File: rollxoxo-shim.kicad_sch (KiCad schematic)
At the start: 70 parts, among them J1 Conn_01x10, J2 USB_C_Receptacle_USB2.0_14P, J3 Conn_01x02, J5 Conn_01x01, J6 Conn_01x10, J7 Conn_01x03, J8 Conn_01x01, SW1 SW_Push, SW2 SW_Push, U1 SN74LV1T125DBV, U2 ESP32-S3FN8, U3 SN74LV1T125DBV, U4 SN74LV1T125DBV, U5 TPSM84338, U6 SN74LV1T125DBV, Y1 48M

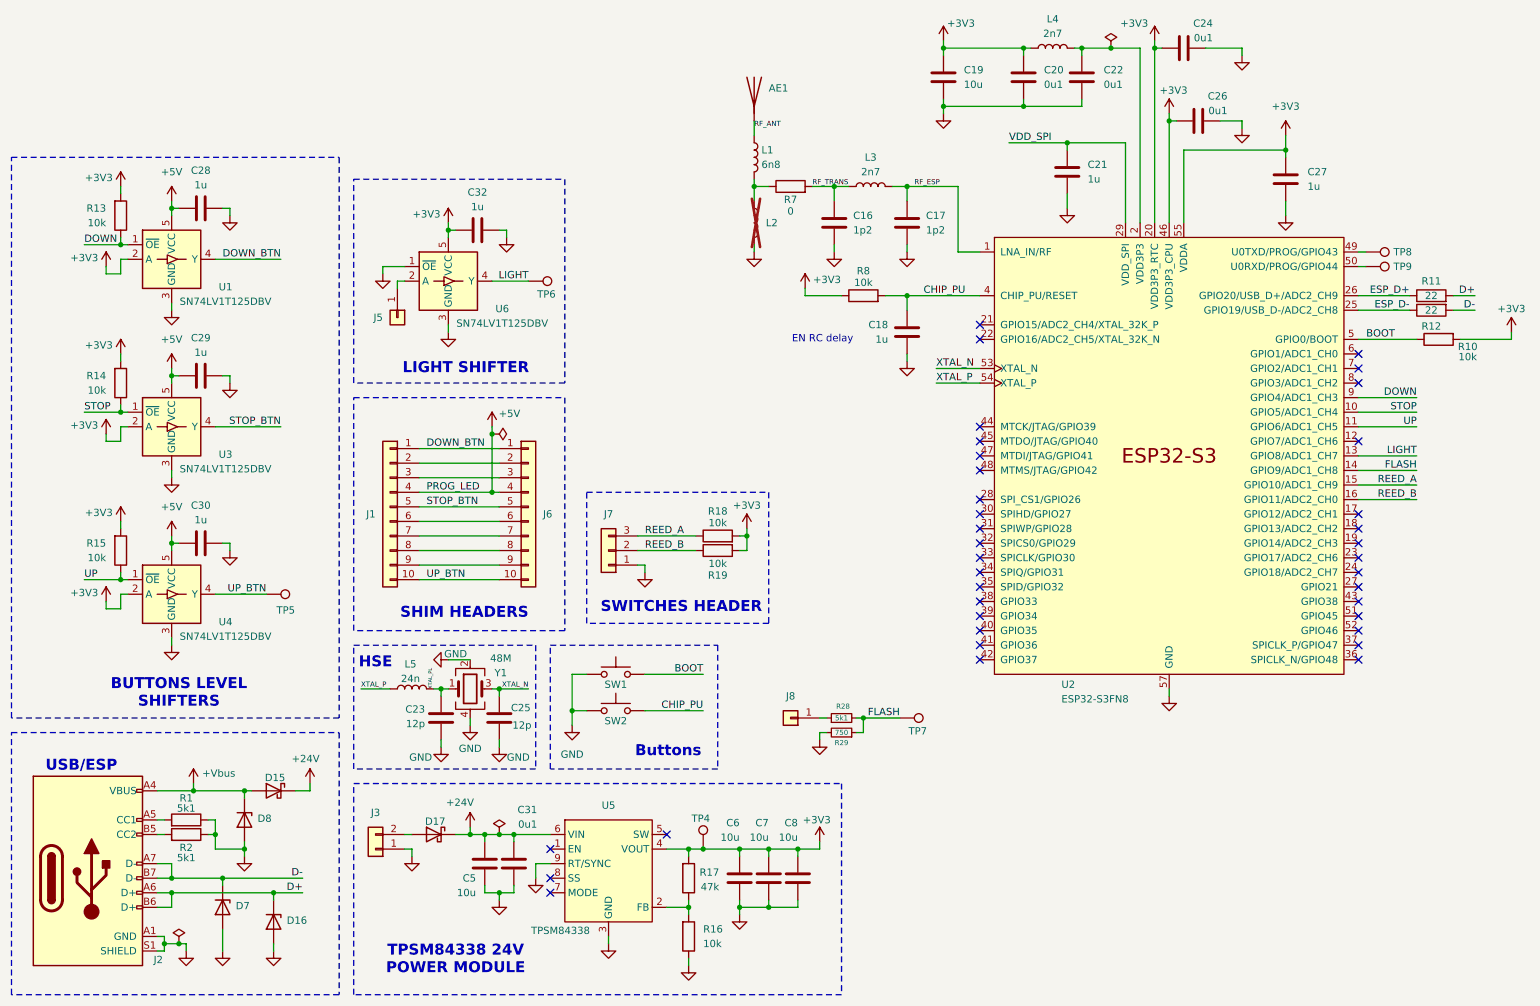
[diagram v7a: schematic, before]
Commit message: schem: renumber
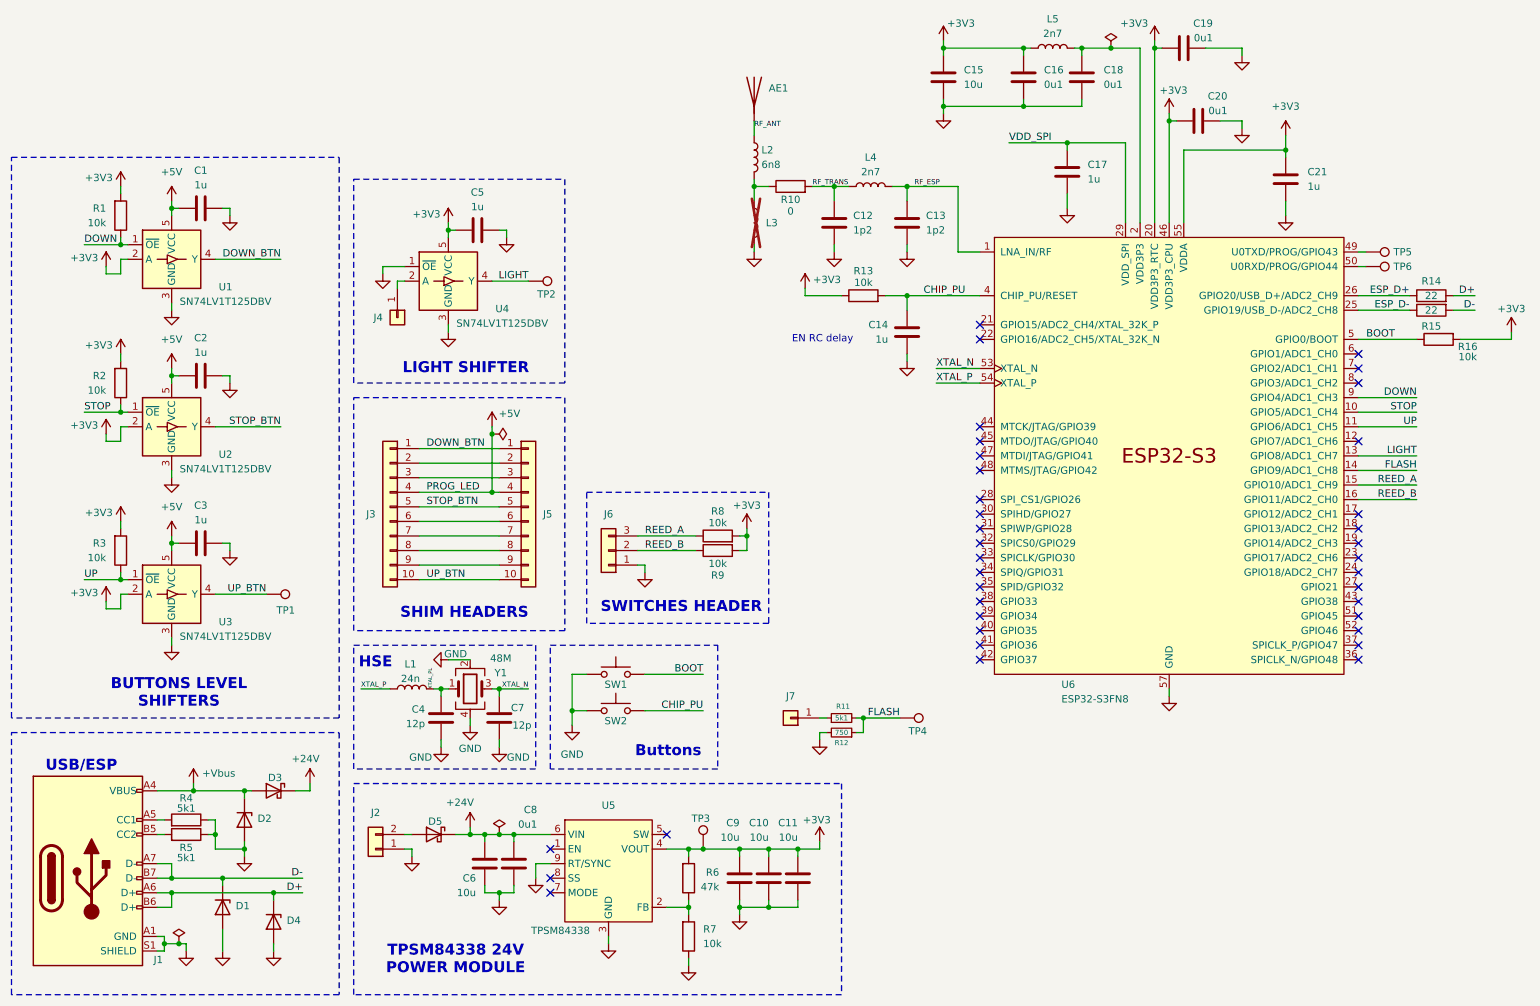
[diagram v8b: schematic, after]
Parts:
- renumbered C28 to C1, C7 to C10, C8 to C11, C16 to C12, C17 to C13, C18 to C14, C19 to C15, C20 to C16, C21 to C17, C22 to C18, C24 to C19, C29 to C2, C26 to C20, C27 to C21, C30 to C3, C23 to C4, C32 to C5, C5 to C6, C25 to C7, C31 to C8, C6 to C9, D7 to D1, D8 to D2, D15 to D3, D16 to D4, D17 to D5, J2 to J1, J3 to J2, J1 to J3, J5 to J4, J6 to J5, J7 to J6, J8 to J7, L5 to L1, L1 to L2, L2 to L3, L3 to L4, L4 to L5, R13 to R1, R7 to R10, R28 to R11, R29 to R12, R8 to R13, R11 to R14, R12 to R15, R10 to R16, R14 to R2, R15 to R3, R1 to R4, R2 to R5, R17 to R6, R16 to R7, R18 to R8, R19 to R9, TP5 to TP1, TP6 to TP2, TP4 to TP3, TP7 to TP4, TP8 to TP5, TP9 to TP6, U3 to U2, U4 to U3, U6 to U4, U2 to U6
